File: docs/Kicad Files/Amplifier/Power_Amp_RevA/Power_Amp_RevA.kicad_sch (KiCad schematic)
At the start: 48 parts, among them J1 Speaker, J2 Input Terminals, J3 Power Input, Q1 2N3904, Q10 QD44H8G, Q2 QD45H8G, Q3 2N3904, Q4 2N3906, Q5 QD44H8G, Q6 2N3904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

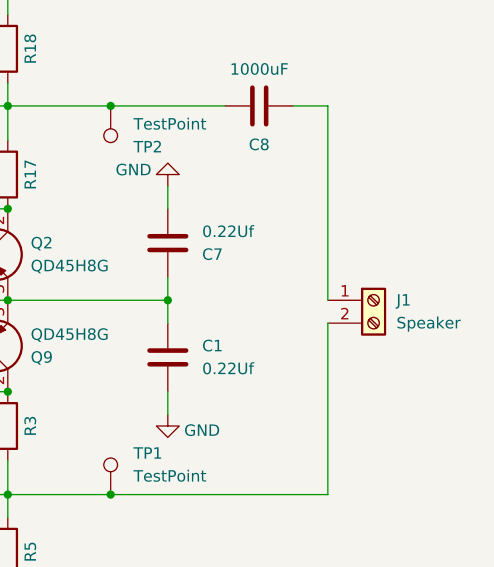
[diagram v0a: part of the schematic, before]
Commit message: changed some footprints per Mark
-routed input traces to back of PCB
-changed footprints of pots and terminal blocks
-flipped terminal blocks so orientation is correct
-added terminal block descriptions
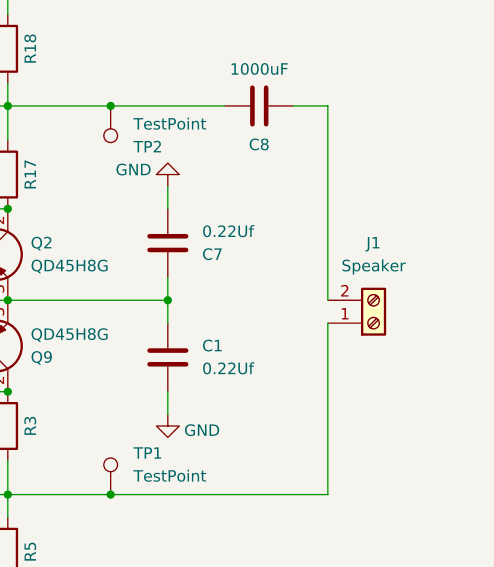
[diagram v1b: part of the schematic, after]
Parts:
- J1, J2, J3: footprint Z_Custom_Footprints:CONN_1935776_PXC -> TerminalBlock_Phoenix:TerminalBlock_Phoenix_MKDS-1,5-2_1x02_P5.00mm_Horizontal
- RV1, RV2: footprint Z_Custom_Footprints:POT_3362P -> Potentiometer_THT:Potentiometer_Bourns_3386P_Vertical
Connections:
- net at C8.2: now also J1.2 (Pin_2); no longer J1.1 (Pin_1)
- net at R3.2, R4.1, R5.1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: now also J1.1 (Pin_1); no longer J1.2 (Pin_2)
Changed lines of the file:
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@@
 			)
 		)
-		(property "Footprint" "Z_Custom_Footprints:CONN_1935776_PXC"
+		(property "Footprint" "TerminalBlock_Phoenix:TerminalBlock_Phoenix_MKDS-1,5-2_1x02_P5.00mm_Horizontal"
 			(at 83.82 83.82 0)
 			(effects
@@
 			)
 		)
-		(property "Footprint" "Z_Custom_Footprints:CONN_1935776_PXC"
+		(property "Footprint" "TerminalBlock_Phoenix:TerminalBlock_Phoenix_MKDS-1,5-2_1x02_P5.00mm_Horizontal"
 			(at 100.33 83.82 0)
 			(effects
@@
 			)
 		)
-		(property "Footprint" "Z_Custom_Footprints:POT_3362P"
+		(property "Footprint" "Potentiometer_THT:Potentiometer_Bourns_3386P_Vertical"
 			(at 110.49 119.38 0)
 			(effects
@@
 	(symbol
 		(lib_id "Connector:Screw_Terminal_01x02")
-		(at 208.28 83.82 0)
-		(unit 1)
-		(exclude_from_sim no)
-		(in_bom yes)
-		(on_board yes)
-		(dnp no)
-		(fields_autoplaced yes)
+		(at 208.28 86.36 0)
+		(mirror x)
+		(unit 1)
+		(exclude_from_sim no)
+		(in_bom yes)
+		(on_board yes)
+		(dnp no)
 		(property "Reference" "J1"
-			(at 210.82 83.8199 0)
-			(effects
-				(font
-					(size 1.27 1.27)
-				)
-				(justify left)
+			(at 208.28 77.47 0)
+			(effects
+				(font
+					(size 1.27 1.27)
+				)
 			)
 		)
 		(property "Value" "Speaker"
-			(at 210.82 86.3599 0)
-			(effects
-				(font
-					(size 1.27 1.27)
-				)
-				(justify left)
-			)
-		)
-		(property "Footprint" "Z_Custom_Footprints:CONN_1935776_PXC"
-			(at 208.28 83.82 0)
+			(at 208.28 80.01 0)
+			(effects
+				(font
+					(size 1.27 1.27)
+				)
+			)
+		)
+		(property "Footprint" "TerminalBlock_Phoenix:TerminalBlock_Phoenix_MKDS-1,5-2_1x02_P5.00mm_Horizontal"
+			(at 208.28 86.36 0)
 			(effects
 				(font
@@
 		)
 		(property "Datasheet" "~"
-			(at 208.28 83.82 0)
+			(at 208.28 86.36 0)
 			(effects
 				(font
@@
 		)
 		(property "Description" "Generic screw terminal, single row, 01x02, script generated (kicad-library-utils/schlib/autogen/connector/)"
-			(at 208.28 83.82 0)
+			(at 208.28 86.36 0)
 			(effects
 				(font
@@
 			)
 		)
-		(property "Footprint" "Z_Custom_Footprints:POT_3362P"
+		(property "Footprint" "Potentiometer_THT:Potentiometer_Bourns_3386P_Vertical"
 			(at 110.49 50.8 0)
 			(effects
